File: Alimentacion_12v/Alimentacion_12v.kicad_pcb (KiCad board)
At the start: 2 copper layers, 58.4 x 43.2 mm, 22 parts, among them J1 USB_B, J2 Conn_01x02_Male, J3 Conn_01x02_Male, J4 Conn_01x02_Male, J5 Conn_01x03_Female, J6 Conn_01x02_Male, U1 lm2577t-15_NOPB, U2 LM317L_TO92

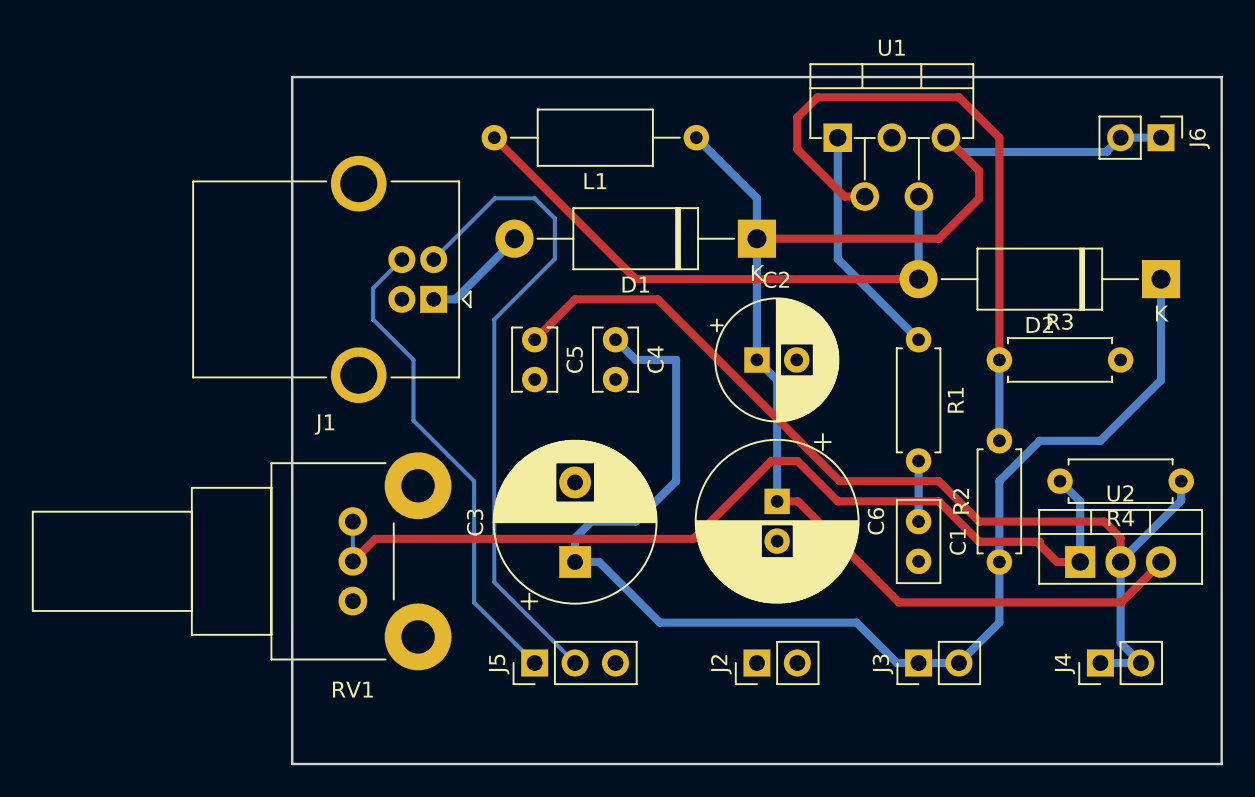
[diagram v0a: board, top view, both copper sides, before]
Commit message: Placa 12V v0.9
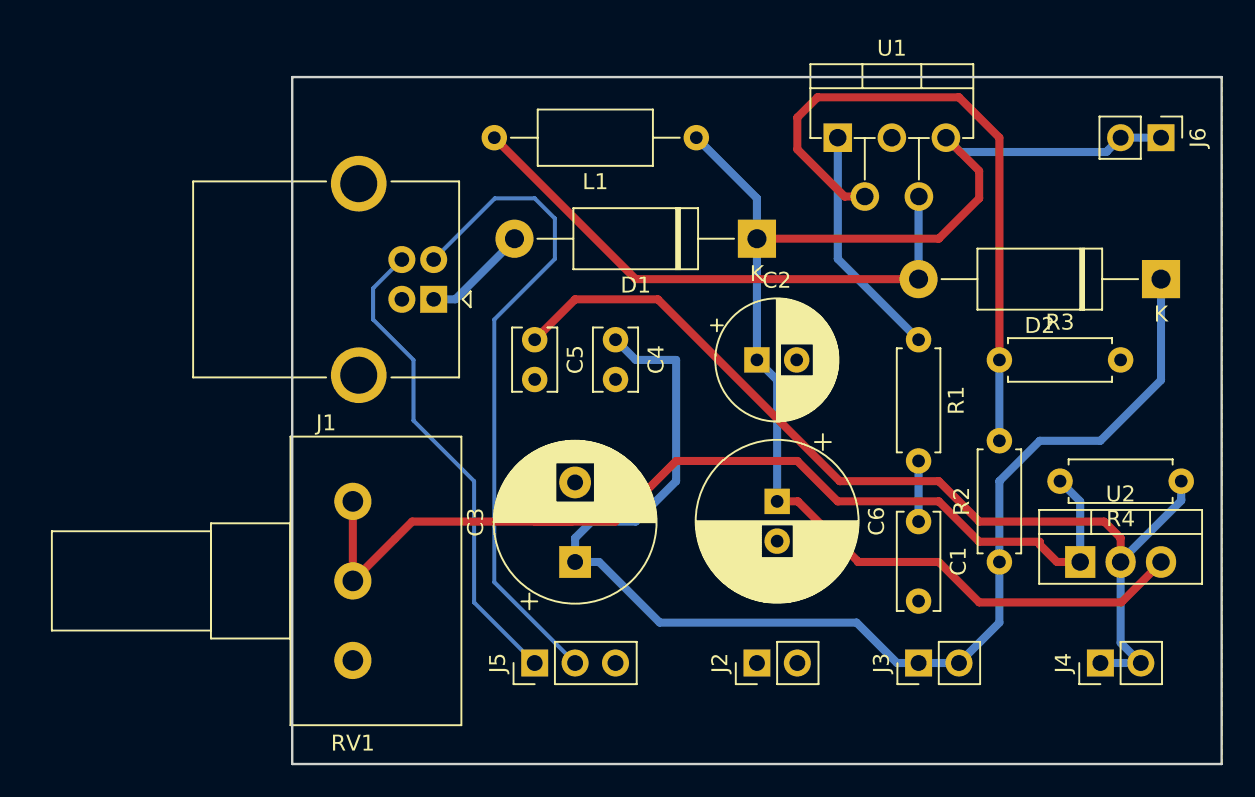
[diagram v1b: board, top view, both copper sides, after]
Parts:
- C1: footprint Capacitor_THT:C_Disc_D5.0mm_W2.5mm_P2.50mm -> Capacitor_THT:C_Disc_D6.0mm_W2.5mm_P5.00mm
- RV1: footprint Potentiometer_THT:Potentiometer_Alps_RK09L_Single_Horizontal -> Potentiometer_THT:Potentiometer_Alps_RK163_Single_Horizontal
- moved RV1 1.27 mm to (49.5, 121.9)
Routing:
- net Net-(R4-Pad2): track 59.2 -> 64.5 mm
